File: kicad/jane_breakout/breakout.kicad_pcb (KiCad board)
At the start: 4 copper layers, 203.2 x 92 mm, 56 parts, among them CON1 BNC_361V504EFT, CON2 BNC_361V504EFT, CON3 BNC_361V504EFT, CON4 BNC_361V504EFT, CON5 BNC_361V504EFT, CON6 BNC_361V504EFT, CON7 BNC_361V504EFT, CON8 BNC_361V504EFT, IC2 74244DW

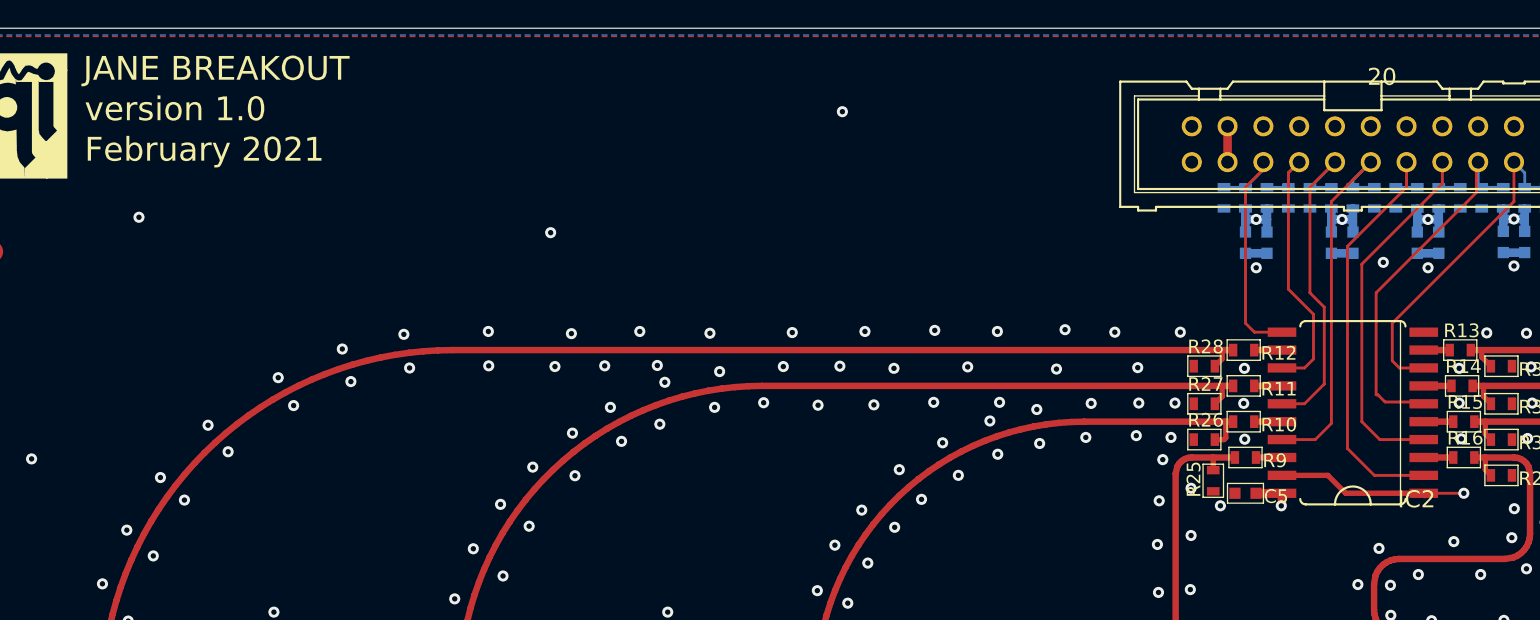
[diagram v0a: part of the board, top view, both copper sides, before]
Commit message: Retouches to the silkscreen
Migrated to version 8 of Kicad.
gerber were generated and sent to fabrication.
Unfortunately the PCB file were overwritten before commiting, so the
current touches to the silkscreen are not isentical to the ones
submitted.
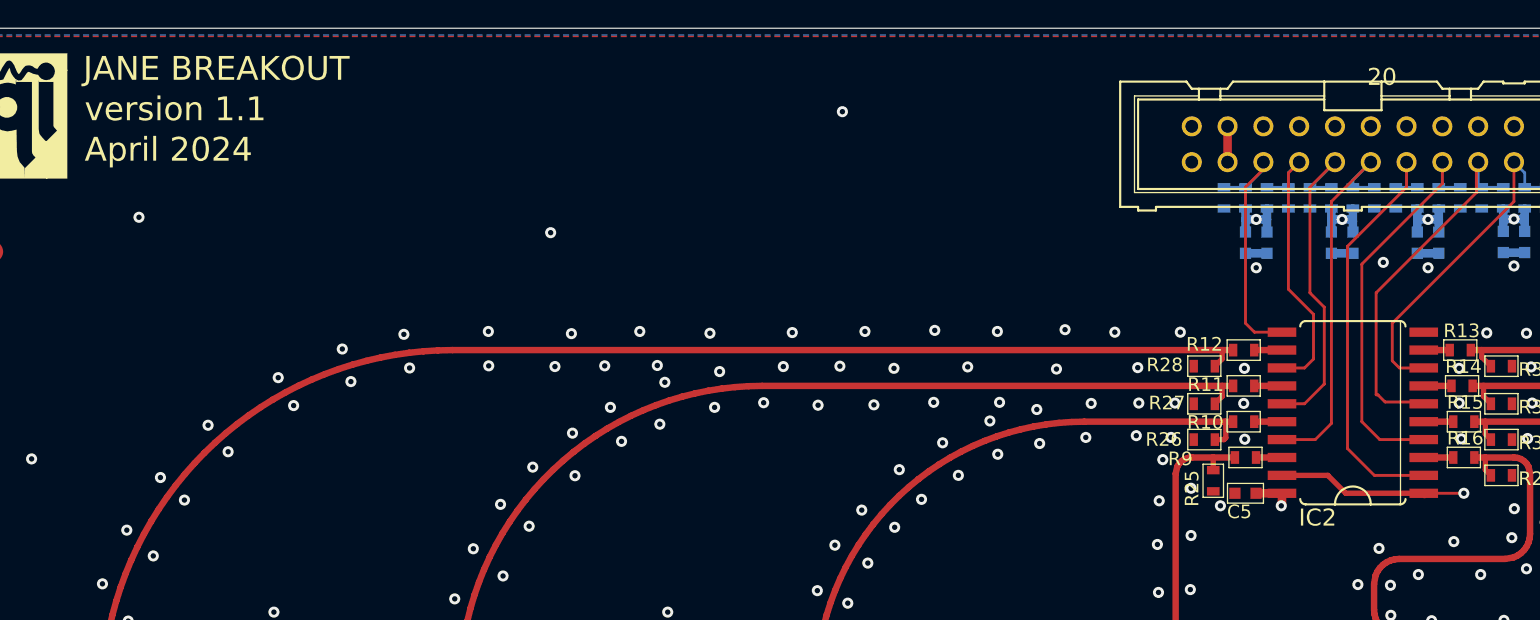
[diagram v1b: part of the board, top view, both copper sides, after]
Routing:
- added copper zone on In2.Cu, net +3V3
- added copper zone on In1.Cu, net GND
- added copper zone on In2.Cu, net GND
- removed copper zone on Route15, net +3V3
- removed copper zone on Route15, net GND
- removed copper zone on Route2, net GND
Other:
- net class Default removed
- board text added: "April 2024"
- board text added: "version 1.1"
- board text removed: "February 2021"
- board text removed: "version 1.0"
